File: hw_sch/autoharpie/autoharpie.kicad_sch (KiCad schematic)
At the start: 0 parts

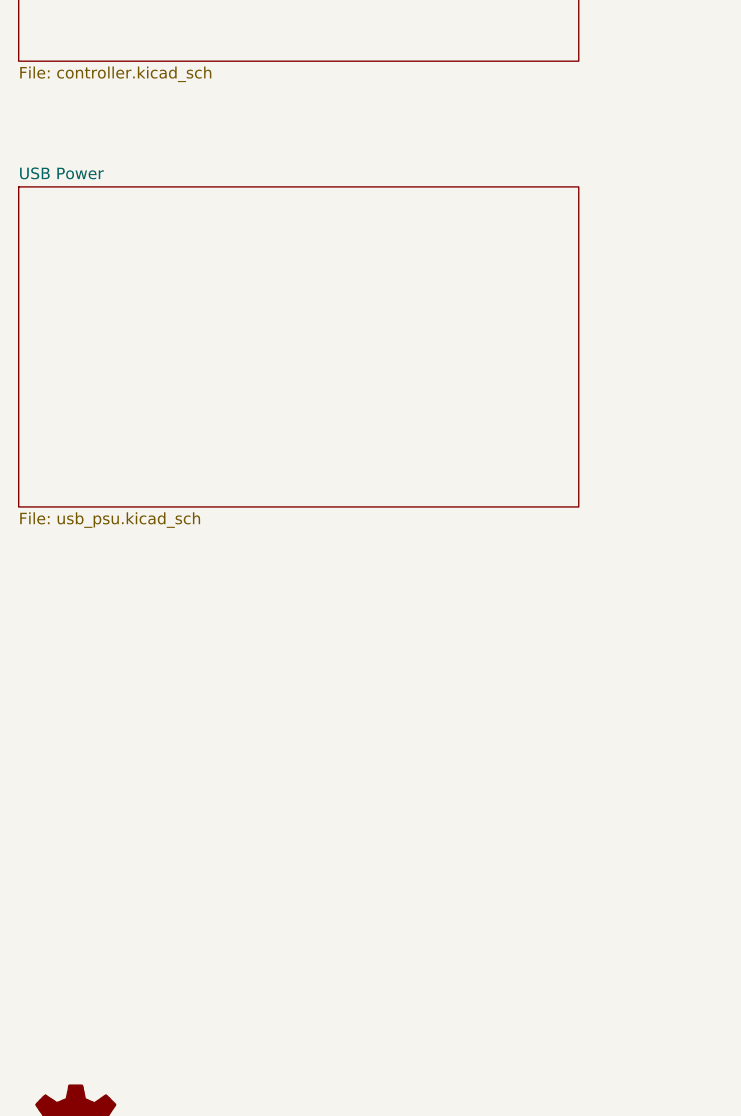
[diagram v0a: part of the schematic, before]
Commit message: teensy mcu chip (imxrt), PSU subsystem work start
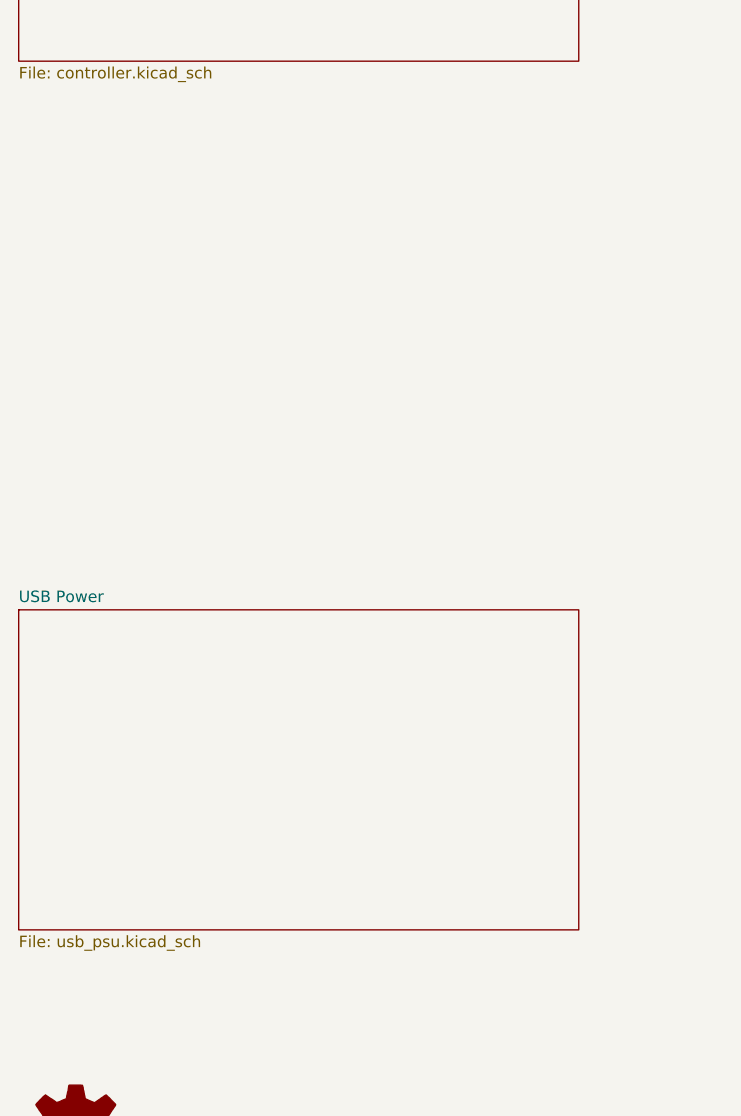
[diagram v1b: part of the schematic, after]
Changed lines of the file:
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@@
     )
   )
-  (sheet (at 33.02 81.28) (size 62.23 35.56) (fields_autoplaced)
+  (sheet (at 33.02 128.27) (size 62.23 35.56) (fields_autoplaced)
     (stroke (width 0.1524) (type solid))
     (fill (color 0 0 0 0.0000))
-    (property "Sheetname" "USB Power" (at 33.02 80.5684 0)
+    (property "Sheetname" "USB Power" (at 33.02 127.5584 0)
       (effects (font (size 1.27 1.27)) (justify left bottom))
     )
-    (property "Sheetfile" "usb_psu.kicad_sch" (at 33.02 117.4246 0)
+    (property "Sheetfile" "usb_psu.kicad_sch" (at 33.02 164.4146 0)
       (effects (font (size 1.27 1.27)) (justify left top))
     )
